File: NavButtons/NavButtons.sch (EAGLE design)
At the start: 7 parts

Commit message: Latest version of NavButtons
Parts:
- removed U$5: JS1300, IntegerLabs:JS1300
- added U$1, U$2, U$6, U$7, U$8: TACT-SWITCH, IntegerLabs:TACT-SWITCH
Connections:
- net BUTTON0: now also U$1.POS1; no longer U$5.A
- net BUTTON1: now also U$2.POS1; no longer U$5.B
- net BUTTON2: now also U$6.POS2; no longer U$5.C
- net BUTTON3: now also U$7.POS1; no longer U$5.D
- net BUTTON4: now also U$8.POS1; no longer U$5.F
- net GND: now also U$1.NEG2, U$2.NEG2, U$6.NEG2, U$7.NEG2, U$8.NEG2; no longer U$5.E, U$5.G, U$5.H, U$5.J, U$5.K
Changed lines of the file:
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@@
 <part name="U$3" library="IntegerLabs" deviceset="TINY841" device=""/>
 <part name="U$4" library="IntegerLabs" deviceset="FOOTPRINT" device=""/>
-<part name="U$5" library="IntegerLabs" deviceset="JS1300" device=""/>
+<part name="U$1" library="IntegerLabs" deviceset="TACT-SWITCH" device=""/>
+<part name="U$2" library="IntegerLabs" deviceset="TACT-SWITCH" device=""/>
+<part name="U$6" library="IntegerLabs" deviceset="TACT-SWITCH" device=""/>
+<part name="U$7" library="IntegerLabs" deviceset="TACT-SWITCH" device=""/>
+<part name="U$8" library="IntegerLabs" deviceset="TACT-SWITCH" device=""/>
 </parts>
 <sheets>
@@
 <instance part="U$3" gate="G$1" x="-50.8" y="101.6"/>
 <instance part="U$4" gate="G$1" x="-68.58" y="60.96"/>
-<instance part="U$5" gate="G$1" x="-111.76" y="124.46"/>
+<instance part="U$1" gate="G$1" x="66.04" y="127"/>
+<instance part="U$2" gate="G$1" x="66.04" y="111.76"/>
+<instance part="U$6" gate="G$1" x="66.04" y="96.52"/>
+<instance part="U$7" gate="G$1" x="66.04" y="81.28"/>
+<instance part="U$8" gate="G$1" x="66.04" y="66.04"/>
 </instances>
 <busses>
@@
 </segment>
 <segment>
-<pinref part="U$5" gate="G$1" pin="E"/>
-<wire x1="-111.76" y1="114.3" x2="-129.54" y2="114.3" width="0.1524" layer="91"/>
-<wire x1="-129.54" y1="114.3" x2="-129.54" y2="109.22" width="0.1524" layer="91"/>
-<pinref part="U$5" gate="G$1" pin="G"/>
-<wire x1="-129.54" y1="109.22" x2="-111.76" y2="109.22" width="0.1524" layer="91"/>
-<pinref part="U$5" gate="G$1" pin="H"/>
-<wire x1="-111.76" y1="109.22" x2="-111.76" y2="106.68" width="0.1524" layer="91"/>
-<pinref part="U$5" gate="G$1" pin="J"/>
-<wire x1="-111.76" y1="104.14" x2="-111.76" y2="106.68" width="0.1524" layer="91"/>
-<pinref part="U$5" gate="G$1" pin="K"/>
-<wire x1="-111.76" y1="104.14" x2="-111.76" y2="101.6" width="0.1524" layer="91"/>
-<wire x1="-111.76" y1="101.6" x2="-111.76" y2="93.98" width="0.1524" layer="91"/>
-<wire x1="-111.76" y1="93.98" x2="-121.92" y2="93.98" width="0.1524" layer="91"/>
-<label x="-121.92" y="93.98" size="1.778" layer="95"/>
+<pinref part="U$1" gate="G$1" pin="NEG2"/>
+<wire x1="66.04" y1="124.46" x2="45.72" y2="124.46" width="0.1524" layer="91"/>
+<label x="45.72" y="124.46" size="1.778" layer="95"/>
+</segment>
+<segment>
+<pinref part="U$2" gate="G$1" pin="NEG2"/>
+<wire x1="66.04" y1="109.22" x2="45.72" y2="109.22" width="0.1524" layer="91"/>
+<label x="45.72" y="109.22" size="1.778" layer="95"/>
+</segment>
+<segment>
+<pinref part="U$6" gate="G$1" pin="NEG2"/>
+<wire x1="66.04" y1="93.98" x2="45.72" y2="93.98" width="0.1524" layer="91"/>
+<label x="45.72" y="93.98" size="1.778" layer="95"/>
+</segment>
+<segment>
+<pinref part="U$7" gate="G$1" pin="NEG2"/>
+<wire x1="66.04" y1="78.74" x2="45.72" y2="78.74" width="0.1524" layer="91"/>
+<label x="45.72" y="78.74" size="1.778" layer="95"/>
+</segment>
+<segment>
+<pinref part="U$8" gate="G$1" pin="NEG2"/>
+<wire x1="66.04" y1="63.5" x2="45.72" y2="63.5" width="0.1524" layer="91"/>
+<label x="45.72" y="63.5" size="1.778" layer="95"/>
 </segment>
 </net>
@@
 </segment>
 <segment>
-<pinref part="U$5" gate="G$1" pin="C"/>
-<wire x1="-111.76" y1="119.38" x2="-119.38" y2="119.38" width="0.1524" layer="91"/>
-<label x="-124.46" y="119.38" size="1.778" layer="95"/>
+<label x="45.72" y="101.6" size="1.778" layer="95"/>
+<wire x1="60.96" y1="101.6" x2="45.72" y2="101.6" width="0.1524" layer="91"/>
+<wire x1="60.96" y1="101.6" x2="60.96" y2="99.06" width="0.1524" layer="91"/>
+<pinref part="U$6" gate="G$1" pin="POS2"/>
+<wire x1="60.96" y1="99.06" x2="66.04" y2="99.06" width="0.1524" layer="91"/>
 </segment>
 </net>
@@
 </segment>
 <segment>
-<pinref part="U$5" gate="G$1" pin="F"/>
-<wire x1="-111.76" y1="111.76" x2="-119.38" y2="111.76" width="0.1524" layer="91"/>
-<label x="-124.46" y="111.76" size="1.778" layer="95"/>
+<pinref part="U$8" gate="G$1" pin="POS1"/>
+<wire x1="66.04" y1="71.12" x2="45.72" y2="71.12" width="0.1524" layer="91"/>
+<label x="45.72" y="71.12" size="1.778" layer="95"/>
 </segment>
 </net>
@@
 </segment>
 <segment>
-<pinref part="U$5" gate="G$1" pin="A"/>
-<wire x1="-111.76" y1="124.46" x2="-119.38" y2="124.46" width="0.1524" layer="91"/>
-<label x="-124.46" y="124.46" size="1.778" layer="95"/>
+<pinref part="U$1" gate="G$1" pin="POS1"/>
+<wire x1="66.04" y1="132.08" x2="45.72" y2="132.08" width="0.1524" layer="91"/>
+<label x="45.72" y="132.08" size="1.778" layer="95"/>
 </segment>
 </net>
@@
 </segment>
 <segment>
-<pinref part="U$5" gate="G$1" pin="D"/>
-<wire x1="-111.76" y1="116.84" x2="-119.38" y2="116.84" width="0.1524" layer="91"/>
-<label x="-124.46" y="116.84" size="1.778" layer="95"/>
+<pinref part="U$7" gate="G$1" pin="POS1"/>
+<wire x1="66.04" y1="86.36" x2="45.72" y2="86.36" width="0.1524" layer="91"/>
+<label x="45.72" y="86.36" size="1.778" layer="95"/>
 </segment>
 </net>
@@
 </segment>
 <segment>
-<pinref part="U$5" gate="G$1" pin="B"/>
-<wire x1="-111.76" y1="121.92" x2="-119.38" y2="121.92" width="0.1524" layer="91"/>
-<label x="-124.46" y="121.92" size="1.778" layer="95"/>
-</segment>
-</net>
+<pinref part="U$2" gate="G$1" pin="POS1"/>
+<wire x1="66.04" y1="116.84" x2="45.72" y2="116.84" width="0.1524" layer="91"/>
+<label x="45.72" y="116.84" size="1.778" layer="95"/>
+</segment>
+</net>

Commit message: Latest version of schematics and boards
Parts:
- removed C2: 10uF, SparkFun-Capacitors:CAP0805
- removed LED: blue, led:LEDCHIPLED_1206
- removed R3: 680, SparkFun-Passives:RESISTOR0805-RES
- removed U$1, U$6, U$7, U$8: TACT-SWITCH, IntegerLabs:TACT-SWITCH
- removed U$3: TINY841, IntegerLabs:TINY841
- removed U$4: FOOTPRINT, IntegerLabs:FOOTPRINT
- added B1, B3, B4, B5, B7: TACT-SWITCH, IntegerLabs:TACT-SWITCH
- added LED1: (no value), adafruit:LEDCHIP-LED0805
- added R1: 680, SparkFun-Passives:RESISTOR0805-RES
- added R2: (no value), SparkFun-Resistors:RESISTOR0805-RES
- added U$5: ATTINY48/88-TQFP, IntegerLabs:ATTINY48/88-TQFP
- C1: value 0.1uF -> .47uF
- U$2: value TACT-SWITCH -> FOOTPRINTFOOTPRINT-2; device IntegerLabs:TACT-SWITCH -> IntegerLabs:FOOTPRINTFOOTPRINT-2
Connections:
- removed net +5V: C1.2, C2.2, U$3.VCC, U$4.+5V
- removed net N$5: LED.A, R3.1
- removed net SCL/SCK: U$3.PA4, U$4.SCL
- removed net SDA/MOSI: U$3.PA6, U$4.SDA
- new net MOSI: U$2.MOSI, U$5.PB3
- new net N$2: R2.2, U$2.VCC
- new net N$8: LED1.A, R1.1
- new net SCK: U$2.SCK, U$5.PB5
- new net SCL: U$2.SCL, U$5.PC5
- new net SDA: U$2.SDA, U$5.PC4
- new net THERM: U$5.PC2
- new net VCC: C1.2, R2.1, U$2.VPROG, U$5.VCC
- net BUTTON0: now also B5.POS1, U$5.PD0; no longer U$1.POS1, U$3.PA0
- net BUTTON1: now also B1.POS1, U$5.PD1; no longer U$2.POS1, U$3.PA1
- net BUTTON2: now also B3.POS1, U$5.PD2; no longer U$3.PA2, U$6.POS2
- net BUTTON3: now also B7.POS2, U$5.PD3; no longer U$3.PA3, U$7.POS1
- net BUTTON4: now also B4.POS1, U$5.PD4; no longer U$3.PA7, U$8.POS1
- net GND: now also B1.NEG2, B3.NEG2, B4.NEG2, B5.NEG2, B7.NEG2, LED1.C, U$2.GND, U$5.GND, U$5.GND@1; no longer C2.1, LED.C, U$1.NEG2, U$2.NEG2, U$3.GND, U$4.GND, U$6.NEG2, U$7.NEG2, U$8.NEG2
- net LED: now also R1.2, U$5.PB1; no longer R3.2, U$3.PB0
- net MISO: now also U$2.MISO, U$5.PB4; no longer U$3.PA5, U$4.MISO
- net RESET: now also U$2.RESET, U$5.PC6; no longer U$3.PB3, U$4.RESET
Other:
- moved on the sheet: C1

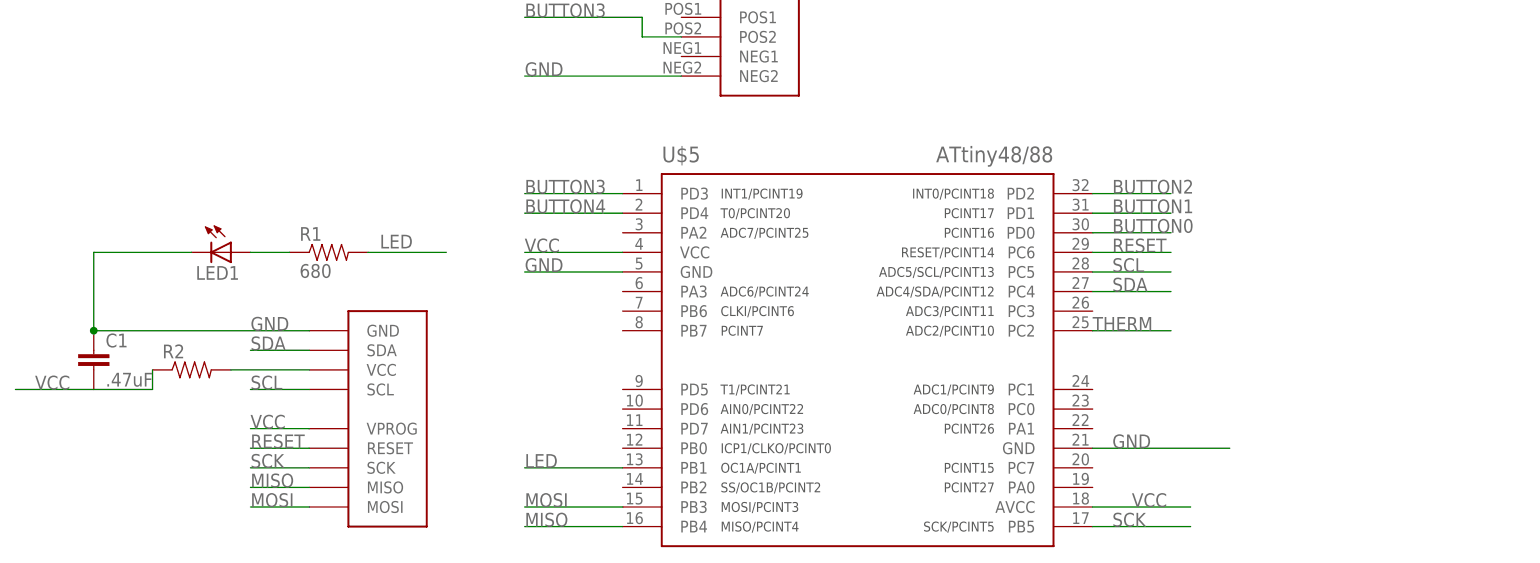
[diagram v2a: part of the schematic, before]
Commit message: Changed NavButtons back to using attiny441
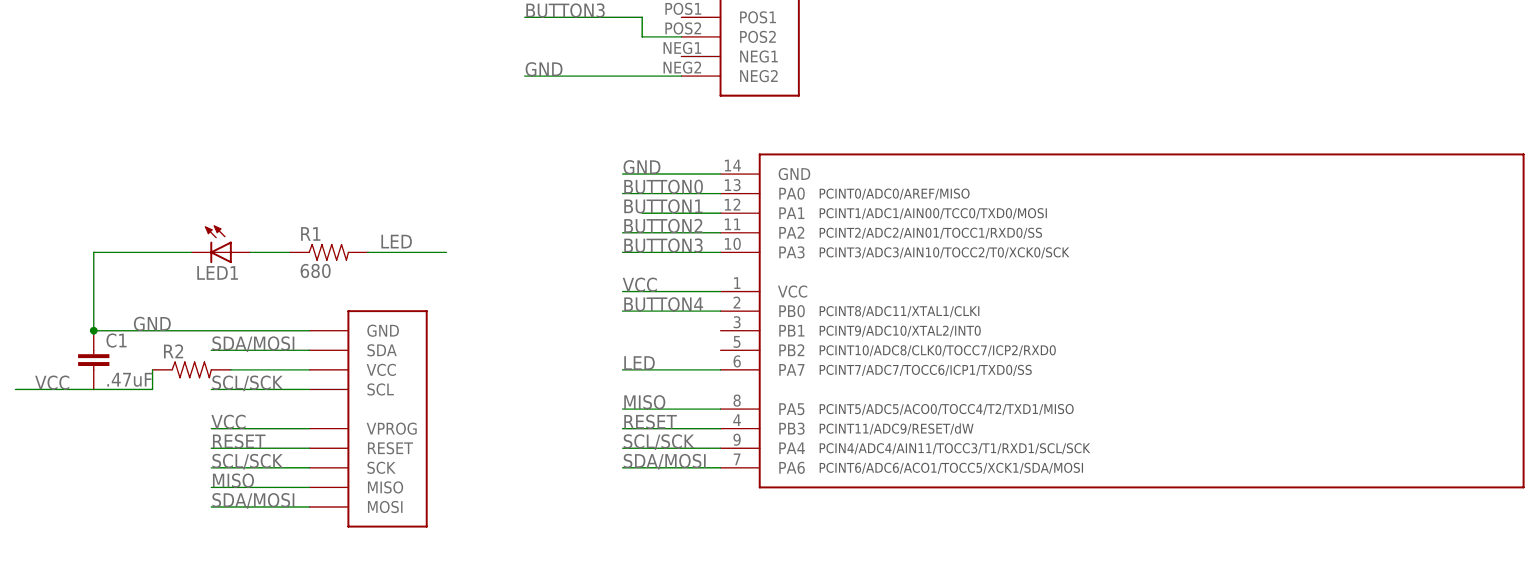
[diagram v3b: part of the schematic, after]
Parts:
- removed U$5: ATTINY48/88-TQFP, IntegerLabs:ATTINY48/88-TQFP
- added U$1: TINY841, IntegerLabs:TINY841
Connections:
- removed net MOSI: U$2.MOSI, U$5.PB3
- removed net SCK: U$2.SCK, U$5.PB5
- removed net SCL: U$2.SCL, U$5.PC5
- removed net SDA: U$2.SDA, U$5.PC4
- removed net THERM: U$5.PC2
- new net SCL/SCK: U$1.PA4, U$2.SCK, U$2.SCL
- new net SDA/MOSI: U$1.PA6, U$2.MOSI, U$2.SDA
- net BUTTON0: now also U$1.PA0; no longer U$5.PD0
- net BUTTON1: now also U$1.PA1; no longer U$5.PD1
- net BUTTON2: now also U$1.PA2; no longer U$5.PD2
- net BUTTON3: now also U$1.PA3; no longer U$5.PD3
- net BUTTON4: now also U$1.PB0; no longer U$5.PD4
- net GND: now also U$1.GND; no longer U$5.GND, U$5.GND@1
- net LED: now also U$1.PA7; no longer U$5.PB1
- net MISO: now also U$1.PA5; no longer U$5.PB4
- net RESET: now also U$1.PB3; no longer U$5.PC6
- net VCC: now also U$1.VCC; no longer U$5.VCC
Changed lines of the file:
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@@
 <part name="R1" library="SparkFun-Passives" deviceset="RESISTOR" device="0805-RES" value="680"/>
 <part name="U$2" library="IntegerLabs" deviceset="FOOTPRINT" device="FOOTPRINT-2" value="FOOTPRINTFOOTPRINT-2"/>
-<part name="U$5" library="IntegerLabs" deviceset="ATTINY48/88" device="-TQFP"/>
 <part name="LED1" library="adafruit" deviceset="LED" device="CHIP-LED0805"/>
 <part name="R2" library="SparkFun-Resistors" deviceset="RESISTOR" device="0805-RES"/>
+<part name="U$1" library="IntegerLabs" deviceset="TINY841" device=""/>
 </parts>
 <sheets>
@@
 <instance part="R1" gate="G$1" x="35.56" y="43.18"/>
 <instance part="U$2" gate="G$1" x="43.18" y="17.78"/>
-<instance part="U$5" gate="G$1" x="104.14" y="30.48"/>
 <instance part="LED1" gate="G$1" x="22.86" y="43.18" rot="R270"/>
 <instance part="R2" gate="G$1" x="17.78" y="27.94"/>
+<instance part="U$1" gate="G$1" x="96.52" y="25.4"/>
 </instances>
 <busses>
@@
 <pinref part="LED1" gate="G$1" pin="C"/>
 <pinref part="U$2" gate="G$1" pin="GND"/>
-<label x="25.4" y="33.02" size="1.778" layer="95"/>
+<label x="10.16" y="33.02" size="1.778" layer="95"/>
 <pinref part="C1" gate="G$1" pin="1"/>
 <wire x1="33.02" y1="33.02" x2="5.08" y2="33.02" width="0.1524" layer="91"/>
@@
 </segment>
 <segment>
-<pinref part="U$5" gate="G$1" pin="GND"/>
-<wire x1="73.66" y1="40.64" x2="60.96" y2="40.64" width="0.1524" layer="91"/>
-<label x="60.96" y="40.64" size="1.778" layer="95"/>
-</segment>
-<segment>
-<pinref part="U$5" gate="G$1" pin="GND@1"/>
-<wire x1="134.62" y1="17.78" x2="152.4" y2="17.78" width="0.1524" layer="91"/>
-<label x="137.16" y="17.78" size="1.778" layer="95"/>
+<wire x1="73.66" y1="53.34" x2="86.36" y2="53.34" width="0.1524" layer="91"/>
+<label x="73.66" y="53.34" size="1.778" layer="95"/>
+<pinref part="U$1" gate="G$1" pin="GND"/>
 </segment>
 </net>
 <net name="RESET" class="0">
 <segment>
-<pinref part="U$5" gate="G$1" pin="PC6"/>
-<wire x1="134.62" y1="43.18" x2="144.78" y2="43.18" width="0.1524" layer="91"/>
-<label x="137.16" y="43.18" size="1.778" layer="95"/>
+<wire x1="73.66" y1="20.32" x2="86.36" y2="20.32" width="0.1524" layer="91"/>
+<label x="73.66" y="20.32" size="1.778" layer="95"/>
+<pinref part="U$1" gate="G$1" pin="PB3"/>
 </segment>
 <segment>
 <pinref part="U$2" gate="G$1" pin="RESET"/>
-<wire x1="33.02" y1="17.78" x2="25.4" y2="17.78" width="0.1524" layer="91"/>
-<label x="25.4" y="17.78" size="1.778" layer="95"/>
+<wire x1="33.02" y1="17.78" x2="20.32" y2="17.78" width="0.1524" layer="91"/>
+<label x="20.32" y="17.78" size="1.778" layer="95"/>
 </segment>
 </net>
 <net name="MISO" class="0">
 <segment>
-<wire x1="73.66" y1="7.62" x2="60.96" y2="7.62" width="0.1524" layer="91"/>
-<pinref part="U$5" gate="G$1" pin="PB4"/>
-<label x="60.96" y="7.62" size="1.778" layer="95"/>
+<wire x1="86.36" y1="22.86" x2="73.66" y2="22.86" width="0.1524" layer="91"/>
+<label x="73.66" y="22.86" size="1.778" layer="95"/>
+<pinref part="U$1" gate="G$1" pin="PA5"/>
 </segment>
 <segment>
 <pinref part="U$2" gate="G$1" pin="MISO"/>
-<wire x1="33.02" y1="12.7" x2="25.4" y2="12.7" width="0.1524" layer="91"/>
-<label x="25.4" y="12.7" size="1.778" layer="95"/>
+<wire x1="33.02" y1="12.7" x2="20.32" y2="12.7" width="0.1524" layer="91"/>
+<label x="20.32" y="12.7" size="1.778" layer="95"/>
 </segment>
 </net>
@@
 </segment>
 <segment>
-<pinref part="U$5" gate="G$1" pin="PB1"/>
-<wire x1="73.66" y1="15.24" x2="60.96" y2="15.24" width="0.1524" layer="91"/>
-<label x="60.96" y="15.24" size="1.778" layer="95"/>
+<wire x1="86.36" y1="27.94" x2="73.66" y2="27.94" width="0.1524" layer="91"/>
+<label x="73.66" y="27.94" size="1.778" layer="95"/>
+<pinref part="U$1" gate="G$1" pin="PA7"/>
 </segment>
 </net>
@@
 </segment>
 <segment>
-<pinref part="U$5" gate="G$1" pin="PD0"/>
-<wire x1="134.62" y1="45.72" x2="144.78" y2="45.72" width="0.1524" layer="91"/>
-<label x="137.16" y="45.72" size="1.778" layer="95"/>
+<wire x1="73.66" y1="50.8" x2="86.36" y2="50.8" width="0.1524" layer="91"/>
+<label x="73.66" y="50.8" size="1.778" layer="95"/>
+<pinref part="U$1" gate="G$1" pin="PA0"/>
 </segment>
 </net>
@@
 </segment>
 <segment>
-<pinref part="U$5" gate="G$1" pin="PD1"/>
-<wire x1="134.62" y1="48.26" x2="144.78" y2="48.26" width="0.1524" layer="91"/>
-<label x="137.16" y="48.26" size="1.778" layer="95"/>
+<wire x1="76.2" y1="48.26" x2="86.36" y2="48.26" width="0.1524" layer="91"/>
+<label x="73.66" y="48.26" size="1.778" layer="95"/>
+<pinref part="U$1" gate="G$1" pin="PA1"/>
 </segment>
 </net>
@@
 </segment>
 <segment>
-<pinref part="U$5" gate="G$1" pin="PD2"/>
-<wire x1="134.62" y1="50.8" x2="144.78" y2="50.8" width="0.1524" layer="91"/>
-<label x="137.16" y="50.8" size="1.778" layer="95"/>
+<wire x1="73.66" y1="45.72" x2="86.36" y2="45.72" width="0.1524" layer="91"/>
+<label x="73.66" y="45.72" size="1.778" layer="95"/>
+<pinref part="U$1" gate="G$1" pin="PA2"/>
 </segment>
 </net>
@@
 </segment>
 <segment>
-<pinref part="U$5" gate="G$1" pin="PD3"/>
-<wire x1="73.66" y1="50.8" x2="60.96" y2="50.8" width="0.1524" layer="91"/>
-<label x="60.96" y="50.8" size="1.778" layer="95"/>
+<wire x1="86.36" y1="43.18" x2="73.66" y2="43.18" width="0.1524" layer="91"/>
+<label x="73.66" y="43.18" size="1.778" layer="95"/>
+<pinref part="U$1" gate="G$1" pin="PA3"/>
 </segment>
 </net>
@@
 </segment>
 <segment>
-<pinref part="U$5" gate="G$1" pin="PD4"/>
-<wire x1="73.66" y1="48.26" x2="60.96" y2="48.26" width="0.1524" layer="91"/>
-<label x="60.96" y="48.26" size="1.778" layer="95"/>
+<wire x1="86.36" y1="35.56" x2="73.66" y2="35.56" width="0.1524" layer="91"/>
+<label x="73.66" y="35.56" size="1.778" layer="95"/>
+<pinref part="U$1" gate="G$1" pin="PB0"/>
 </segment>
 </net>
@@
 <segment>
 <pinref part="U$2" gate="G$1" pin="VPROG"/>
-<wire x1="33.02" y1="20.32" x2="25.4" y2="20.32" width="0.1524" layer="91"/>
-<label x="25.4" y="20.32" size="1.778" layer="95"/>
-</segment>
-<segment>
-<pinref part="U$5" gate="G$1" pin="VCC"/>
-<wire x1="73.66" y1="43.18" x2="60.96" y2="43.18" width="0.1524" layer="91"/>
-<label x="60.96" y="43.18" size="1.778" layer="95"/>
-</segment>
-<segment>
-<wire x1="134.62" y1="10.16" x2="147.32" y2="10.16" width="0.1524" layer="91"/>
-<label x="139.7" y="10.16" size="1.778" layer="95"/>
-</segment>
-</net>
-<net name="SCK" class="0">
-<segment>
-<pinref part="U$2" gate="G$1" pin="SCK"/>
-<wire x1="33.02" y1="15.24" x2="25.4" y2="15.24" width="0.1524" layer="91"/>
-<label x="25.4" y="15.24" size="1.778" layer="95"/>
-</segment>
-<segment>
-<pinref part="U$5" gate="G$1" pin="PB5"/>
-<wire x1="134.62" y1="7.62" x2="147.32" y2="7.62" width="0.1524" layer="91"/>
-<label x="137.16" y="7.62" size="1.778" layer="95"/>
-</segment>
-</net>
-<net name="MOSI" class="0">
-<segment>
-<pinref part="U$2" gate="G$1" pin="MOSI"/>
-<wire x1="33.02" y1="10.16" x2="25.4" y2="10.16" width="0.1524" layer="91"/>
-<label x="25.4" y="10.16" size="1.778" layer="95"/>
-</segment>
-<segment>
-<pinref part="U$5" gate="G$1" pin="PB3"/>
-<wire x1="73.66" y1="10.16" x2="60.96" y2="10.16" width="0.1524" layer="91"/>
-<label x="60.96" y="10.16" size="1.778" layer="95"/>
-</segment>
-</net>
-<net name="SDA" class="0">
-<segment>
-<pinref part="U$5" gate="G$1" pin="PC4"/>
-<wire x1="134.62" y1="38.1" x2="144.78" y2="38.1" width="0.1524" layer="91"/>
-<label x="137.16" y="38.1" size="1.778" layer="95"/>
-</segment>
-<segment>
-<pinref part="U$2" gate="G$1" pin="SDA"/>
-<wire x1="33.02" y1="30.48" x2="25.4" y2="30.48" width="0.1524" layer="91"/>
-<label x="25.4" y="30.48" size="1.778" layer="95"/>
-</segment>
-</net>
-<net name="SCL" class="0">
-<segment>
-<wire x1="134.62" y1="40.64" x2="144.78" y2="40.64" width="0.1524" layer="91"/>
-<pinref part="U$5" gate="G$1" pin="PC5"/>
-<label x="137.16" y="40.64" size="1.778" layer="95"/>
-</segment>
-<segment>
-<pinref part="U$2" gate="G$1" pin="SCL"/>
-<wire x1="33.02" y1="25.4" x2="25.4" y2="25.4" width="0.1524" layer="91"/>
-<label x="25.4" y="25.4" size="1.778" layer="95"/>
+<wire x1="33.02" y1="20.32" x2="20.32" y2="20.32" width="0.1524" layer="91"/>
+<label x="20.32" y="20.32" size="1.778" layer="95"/>
+</segment>
+<segment>
+<wire x1="73.66" y1="38.1" x2="86.36" y2="38.1" width="0.1524" layer="91"/>
+<label x="73.66" y="38.1" size="1.778" layer="95"/>
+<pinref part="U$1" gate="G$1" pin="VCC"/>
 </segment>
 </net>
@@
 </segment>
 </net>
-<net name="THERM" class="0">
-<segment>
-<pinref part="U$5" gate="G$1" pin="PC2"/>
-<wire x1="134.62" y1="33.02" x2="144.78" y2="33.02" width="0.1524" layer="91"/>
-<label x="134.62" y="33.02" size="1.778" layer="95"/>
-</segment>
-</net>
 <net name="N$2" class="0">
 <segment>
@@
 </segment>
 </net>
+<net name="SCL/SCK" class="0">
+<segment>
+<wire x1="73.66" y1="17.78" x2="86.36" y2="17.78" width="0.1524" layer="91"/>
+<label x="73.66" y="17.78" size="1.778" layer="95"/>
+<pinref part="U$1" gate="G$1" pin="PA4"/>
+</segment>
+<segment>
+<pinref part="U$2" gate="G$1" pin="SCL"/>
+<wire x1="33.02" y1="25.4" x2="20.32" y2="25.4" width="0.1524" layer="91"/>
+<label x="20.32" y="25.4" size="1.778" layer="95"/>
+</segment>
+<segment>
+<pinref part="U$2" gate="G$1" pin="SCK"/>
+<wire x1="33.02" y1="15.24" x2="20.32" y2="15.24" width="0.1524" layer="91"/>
+<label x="20.32" y="15.24" size="1.778" layer="95"/>
+</segment>
+</net>
+<net name="SDA/MOSI" class="0">
+<segment>
+<wire x1="86.36" y1="15.24" x2="73.66" y2="15.24" width="0.1524" layer="91"/>
+<label x="73.66" y="15.24" size="1.778" layer="95"/>
+<pinref part="U$1" gate="G$1" pin="PA6"/>
+</segment>
+<segment>
+<pinref part="U$2" gate="G$1" pin="MOSI"/>
+<wire x1="33.02" y1="10.16" x2="20.32" y2="10.16" width="0.1524" layer="91"/>
+<label x="20.32" y="10.16" size="1.778" layer="95"/>
+</segment>
+<segment>
+<pinref part="U$2" gate="G$1" pin="SDA"/>
+<wire x1="33.02" y1="30.48" x2="20.32" y2="30.48" width="0.1524" layer="91"/>
+<label x="20.32" y="30.48" size="1.778" layer="95"/>
+</segment>
+</net>
